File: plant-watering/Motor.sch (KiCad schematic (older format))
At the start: 3 parts, among them J5 Screw_Terminal_01x02, J6 Screw_Terminal_01x02, J7 Screw_Terminal_01x02

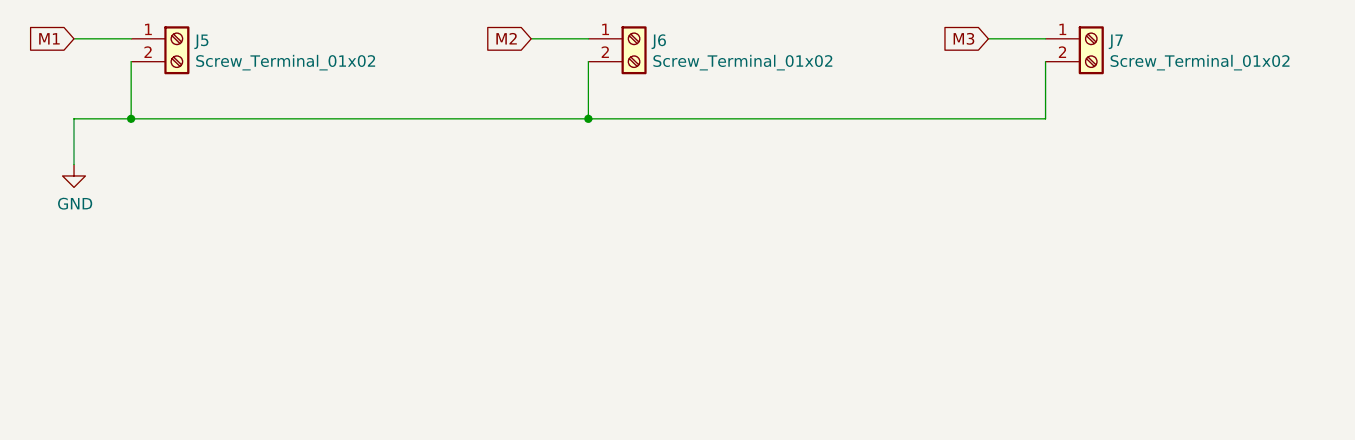
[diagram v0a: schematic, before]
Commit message: edited schematic & started pcb design
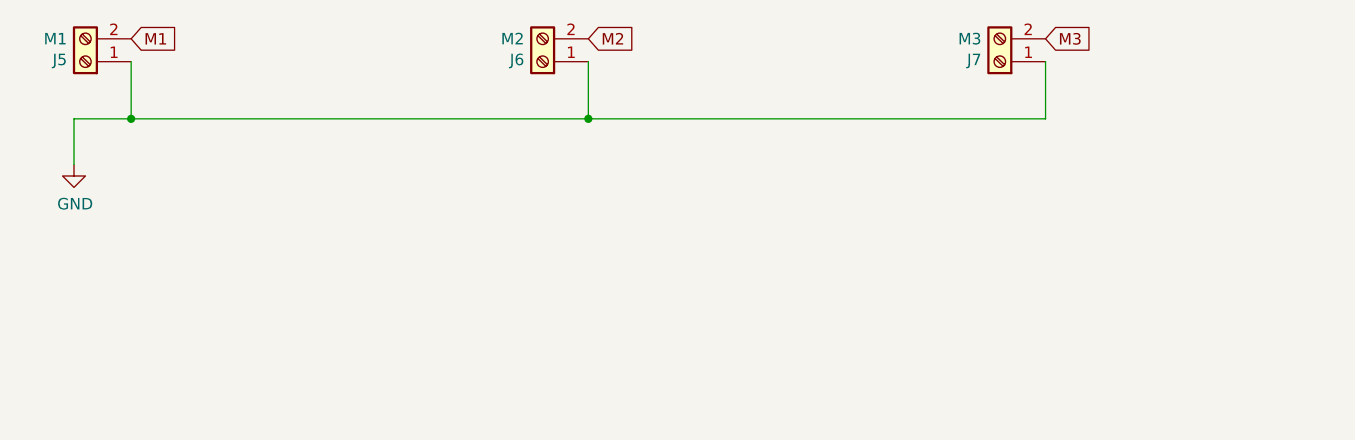
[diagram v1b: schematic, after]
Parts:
- J5: value Screw_Terminal_01x02 -> M1
- J6: value Screw_Terminal_01x02 -> M2
- J7: value Screw_Terminal_01x02 -> M3
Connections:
- net GND: now also J5.1 (Pin_1), J6.1 (Pin_1), J7.1 (Pin_1); no longer J5.2 (Pin_2), J6.2 (Pin_2), J7.2 (Pin_2)
- net M1: now also J5.2 (Pin_2); no longer J5.1 (Pin_1)
- net M2: now also J6.2 (Pin_2); no longer J6.1 (Pin_1)
- net M3: now also J7.2 (Pin_2); no longer J7.1 (Pin_1)
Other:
- moved on the sheet: J5, J6, J7
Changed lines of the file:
@@
 L Connector:Screw_Terminal_01x02 J5
 U 1 1 600B60F0
-P 4700 2900
-F 0 "J5" H 4780 2892 50  0000 L CNN
-F 1 "Screw_Terminal_01x02" H 4780 2801 50  0000 L CNN
-F 2 "Terminal_Blocks:TerminalBlock_bornier-2_P5.08mm" H 4700 2900 50  0001 C CNN
-F 3 "~" H 4700 2900 50  0001 C CNN
-	1    4700 2900
-	1    0    0    -1
+P 4300 3000
+F 0 "J5" H 4380 2992 50  0000 L CNN
+F 1 "M1" H 4380 2901 50  0000 L CNN
+F 2 "Terminal_Blocks:TerminalBlock_bornier-2_P5.08mm" H 4300 3000 50  0001 C CNN
+F 3 "~" H 4300 3000 50  0001 C CNN
+	1    4300 3000
+	-1   0    0    1
 $EndComp
 $Comp
 L Connector:Screw_Terminal_01x02 J6
 U 1 1 600B6A4A
-P 6700 2900
-F 0 "J6" H 6780 2892 50  0000 L CNN
-F 1 "Screw_Terminal_01x02" H 6780 2801 50  0000 L CNN
-F 2 "Terminal_Blocks:TerminalBlock_bornier-2_P5.08mm" H 6700 2900 50  0001 C CNN
-F 3 "~" H 6700 2900 50  0001 C CNN
-	1    6700 2900
-	1    0    0    -1
+P 6300 3000
+F 0 "J6" H 6380 2992 50  0000 L CNN
+F 1 "M2" H 6380 2901 50  0000 L CNN
+F 2 "Terminal_Blocks:TerminalBlock_bornier-2_P5.08mm" H 6300 3000 50  0001 C CNN
+F 3 "~" H 6300 3000 50  0001 C CNN
+	1    6300 3000
+	-1   0    0    1
 $EndComp
 $Comp
 L Connector:Screw_Terminal_01x02 J7
 U 1 1 600B7436
-P 8700 2900
-F 0 "J7" H 8780 2892 50  0000 L CNN
-F 1 "Screw_Terminal_01x02" H 8780 2801 50  0000 L CNN
-F 2 "Terminal_Blocks:TerminalBlock_bornier-2_P5.08mm" H 8700 2900 50  0001 C CNN
-F 3 "~" H 8700 2900 50  0001 C CNN
-	1    8700 2900
-	1    0    0    -1
+P 8300 3000
+F 0 "J7" H 8380 2992 50  0000 L CNN
+F 1 "M3" H 8380 2901 50  0000 L CNN
+F 2 "Terminal_Blocks:TerminalBlock_bornier-2_P5.08mm" H 8300 3000 50  0001 C CNN
+F 3 "~" H 8300 3000 50  0001 C CNN
+	1    8300 3000
+	-1   0    0    1
 $EndComp
 Wire Wire Line
@@
 	1    0    0    -1
 $EndComp
-Text GLabel 4250 2900 0    50   Input ~ 0
+Text GLabel 4500 2900 2    50   Input ~ 0
 M1
-Text GLabel 6250 2900 0    50   Input ~ 0
+Text GLabel 6500 2900 2    50   Input ~ 0
 M2
-Text GLabel 8250 2900 0    50   Input ~ 0
+Text GLabel 8500 2900 2    50   Input ~ 0
 M3
-Wire Wire Line
-	8250 2900 8500 2900
-Wire Wire Line
-	6500 2900 6250 2900
-Wire Wire Line
-	4500 2900 4250 2900
 $EndSCHEMATC

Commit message: added several parts#
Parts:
- added J11: M1, Terminal_Blocks:TerminalBlock_bornier-2_P5.08mm, symbol Connector:Screw_Terminal_01x02
- added J12: M2, Terminal_Blocks:TerminalBlock_bornier-2_P5.08mm, symbol Connector:Screw_Terminal_01x02
- added J13: M3, Terminal_Blocks:TerminalBlock_bornier-2_P5.08mm, symbol Connector:Screw_Terminal_01x02
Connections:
- net GND: now also J11.1 (Pin_1), J12.1 (Pin_1), J13.1 (Pin_1)
- new net M4: J11.2 (Pin_2)
- new net M5: J12.2 (Pin_2)
- new net M6: J13.2 (Pin_2)
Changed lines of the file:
@@
 $Descr A4 11693 8268
 encoding utf-8
-Sheet 6 6
+Sheet 6 7
 Title ""
 Date ""
@@
 Text GLabel 8500 2900 2    50   Input ~ 0
 M3
+$Comp
+L Connector:Screw_Terminal_01x02 J11
+U 1 1 60129D25
+P 4300 3900
+F 0 "J11" H 4380 3892 50  0000 L CNN
+F 1 "M1" H 4380 3801 50  0000 L CNN
+F 2 "Terminal_Blocks:TerminalBlock_bornier-2_P5.08mm" H 4300 3900 50  0001 C CNN
+F 3 "~" H 4300 3900 50  0001 C CNN
+	1    4300 3900
+	-1   0    0    1
+$EndComp
+$Comp
+L Connector:Screw_Terminal_01x02 J12
+U 1 1 60129D2B
+P 6300 3900
+F 0 "J12" H 6380 3892 50  0000 L CNN
+F 1 "M2" H 6380 3801 50  0000 L CNN
+F 2 "Terminal_Blocks:TerminalBlock_bornier-2_P5.08mm" H 6300 3900 50  0001 C CNN
+F 3 "~" H 6300 3900 50  0001 C CNN
+	1    6300 3900
+	-1   0    0    1
+$EndComp
+$Comp
+L Connector:Screw_Terminal_01x02 J13
+U 1 1 60129D31
+P 8300 3900
+F 0 "J13" H 8380 3892 50  0000 L CNN
+F 1 "M3" H 8380 3801 50  0000 L CNN
+F 2 "Terminal_Blocks:TerminalBlock_bornier-2_P5.08mm" H 8300 3900 50  0001 C CNN
+F 3 "~" H 8300 3900 50  0001 C CNN
+	1    8300 3900
+	-1   0    0    1
+$EndComp
+Wire Wire Line
+	8500 3900 8500 4150
+Wire Wire Line
+	8500 4150 6500 4150
+Wire Wire Line
+	4500 3900 4500 4150
+Connection ~ 4500 4150
+Wire Wire Line
+	4500 4150 4250 4150
+Wire Wire Line
+	6500 3900 6500 4150
+Connection ~ 6500 4150
+Wire Wire Line
+	6500 4150 4500 4150
+Wire Wire Line
+	4250 4150 4250 4350
+$Comp
+L power:GND #PWR0112
+U 1 1 60129D40
+P 4250 4350
+F 0 "#PWR0112" H 4250 4100 50  0001 C CNN
+F 1 "GND" H 4255 4177 50  0000 C CNN
+F 2 "" H 4250 4350 50  0001 C CNN
+F 3 "" H 4250 4350 50  0001 C CNN
+	1    4250 4350
+	1    0    0    -1
+$EndComp
+Text GLabel 4500 3800 2    50   Input ~ 0
+M4
+Text GLabel 6500 3800 2    50   Input ~ 0
+M5
+Text GLabel 8500 3800 2    50   Input ~ 0
+M6
 $EndSCHEMATC

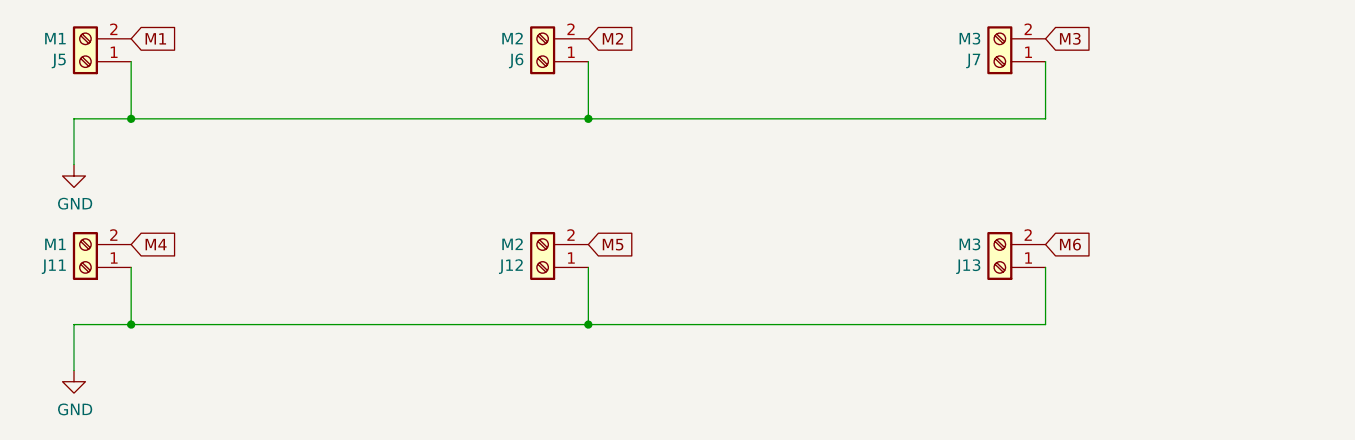
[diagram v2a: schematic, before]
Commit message: changed pcb parts
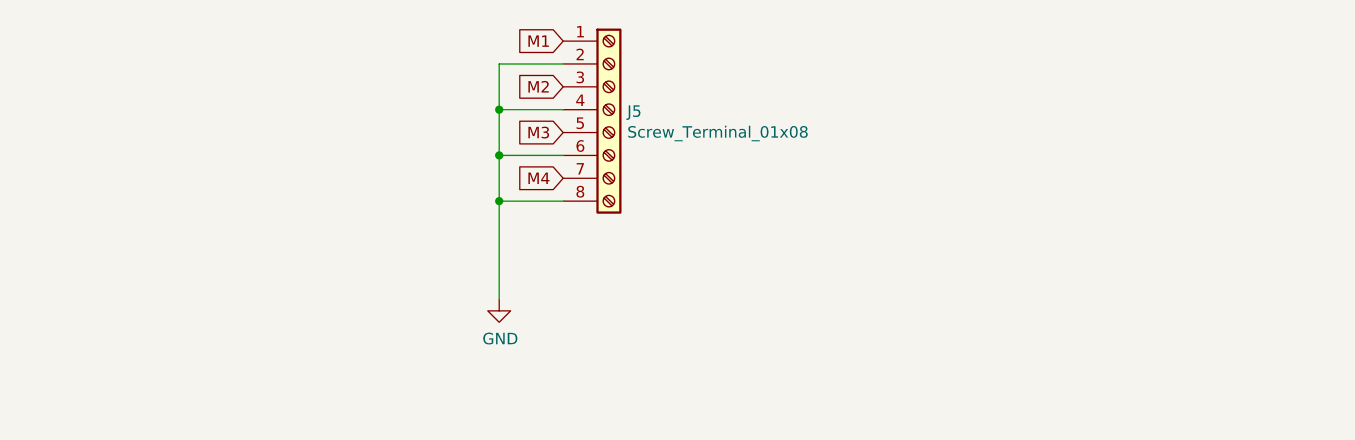
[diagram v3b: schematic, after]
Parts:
- removed J11, J5: M1, Terminal_Blocks:TerminalBlock_bornier-2_P5.08mm, symbol Connector:Screw_Terminal_01x02
- removed J12, J6: M2, Terminal_Blocks:TerminalBlock_bornier-2_P5.08mm, symbol Connector:Screw_Terminal_01x02
- removed J13, J7: M3, Terminal_Blocks:TerminalBlock_bornier-2_P5.08mm, symbol Connector:Screw_Terminal_01x02
- added J5: Screw_Terminal_01x08, TerminalBlock:ScrewTerminal_1x8_P5.00, symbol Connector:Screw_Terminal_01x08
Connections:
- net GND: now also J5.2 (Pin_2), J5.4 (Pin_4), J5.6 (Pin_6), J5.8 (Pin_8)
- net M1: now also J5.1 (Pin_1)
- net M2: now also J5.3 (Pin_3)
- net M3: now also J5.5 (Pin_5)
- net M4: now also J5.7 (Pin_7)
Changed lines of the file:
@@
 Comment4 ""
 $EndDescr
-$Comp
-L Connector:Screw_Terminal_01x02 J5
-U 1 1 600B60F0
-P 4300 3000
-F 0 "J5" H 4380 2992 50  0000 L CNN
-F 1 "M1" H 4380 2901 50  0000 L CNN
-F 2 "Terminal_Blocks:TerminalBlock_bornier-2_P5.08mm" H 4300 3000 50  0001 C CNN
-F 3 "~" H 4300 3000 50  0001 C CNN
-	1    4300 3000
-	-1   0    0    1
-$EndComp
-$Comp
-L Connector:Screw_Terminal_01x02 J6
-U 1 1 600B6A4A
-P 6300 3000
-F 0 "J6" H 6380 2992 50  0000 L CNN
-F 1 "M2" H 6380 2901 50  0000 L CNN
-F 2 "Terminal_Blocks:TerminalBlock_bornier-2_P5.08mm" H 6300 3000 50  0001 C CNN
-F 3 "~" H 6300 3000 50  0001 C CNN
-	1    6300 3000
-	-1   0    0    1
-$EndComp
-$Comp
-L Connector:Screw_Terminal_01x02 J7
-U 1 1 600B7436
-P 8300 3000
-F 0 "J7" H 8380 2992 50  0000 L CNN
-F 1 "M3" H 8380 2901 50  0000 L CNN
-F 2 "Terminal_Blocks:TerminalBlock_bornier-2_P5.08mm" H 8300 3000 50  0001 C CNN
-F 3 "~" H 8300 3000 50  0001 C CNN
-	1    8300 3000
-	-1   0    0    1
-$EndComp
-Wire Wire Line
-	8500 3000 8500 3250
-Wire Wire Line
-	8500 3250 6500 3250
-Wire Wire Line
-	4500 3000 4500 3250
-Connection ~ 4500 3250
-Wire Wire Line
-	4500 3250 4250 3250
-Wire Wire Line
-	6500 3000 6500 3250
-Connection ~ 6500 3250
-Wire Wire Line
-	6500 3250 4500 3250
-Wire Wire Line
-	4250 3250 4250 3450
-$Comp
-L power:GND #PWR0107
-U 1 1 600B8A6F
-P 4250 3450
-F 0 "#PWR0107" H 4250 3200 50  0001 C CNN
-F 1 "GND" H 4255 3277 50  0000 C CNN
-F 2 "" H 4250 3450 50  0001 C CNN
-F 3 "" H 4250 3450 50  0001 C CNN
-	1    4250 3450
-	1    0    0    -1
-$EndComp
-Text GLabel 4500 2900 2    50   Input ~ 0
+Text GLabel 6390 2910 0    50   Input ~ 0
 M1
-Text GLabel 6500 2900 2    50   Input ~ 0
+Text GLabel 6390 3110 0    50   Input ~ 0
 M2
-Text GLabel 8500 2900 2    50   Input ~ 0
+Text GLabel 6390 3310 0    50   Input ~ 0
 M3
-$Comp
-L Connector:Screw_Terminal_01x02 J11
-U 1 1 60129D25
-P 4300 3900
-F 0 "J11" H 4380 3892 50  0000 L CNN
-F 1 "M1" H 4380 3801 50  0000 L CNN
-F 2 "Terminal_Blocks:TerminalBlock_bornier-2_P5.08mm" H 4300 3900 50  0001 C CNN
-F 3 "~" H 4300 3900 50  0001 C CNN
-	1    4300 3900
-	-1   0    0    1
-$EndComp
-$Comp
-L Connector:Screw_Terminal_01x02 J12
-U 1 1 60129D2B
-P 6300 3900
-F 0 "J12" H 6380 3892 50  0000 L CNN
-F 1 "M2" H 6380 3801 50  0000 L CNN
-F 2 "Terminal_Blocks:TerminalBlock_bornier-2_P5.08mm" H 6300 3900 50  0001 C CNN
-F 3 "~" H 6300 3900 50  0001 C CNN
-	1    6300 3900
-	-1   0    0    1
-$EndComp
-$Comp
-L Connector:Screw_Terminal_01x02 J13
-U 1 1 60129D31
-P 8300 3900
-F 0 "J13" H 8380 3892 50  0000 L CNN
-F 1 "M3" H 8380 3801 50  0000 L CNN
-F 2 "Terminal_Blocks:TerminalBlock_bornier-2_P5.08mm" H 8300 3900 50  0001 C CNN
-F 3 "~" H 8300 3900 50  0001 C CNN
-	1    8300 3900
-	-1   0    0    1
-$EndComp
-Wire Wire Line
-	8500 3900 8500 4150
-Wire Wire Line
-	8500 4150 6500 4150
-Wire Wire Line
-	4500 3900 4500 4150
-Connection ~ 4500 4150
-Wire Wire Line
-	4500 4150 4250 4150
-Wire Wire Line
-	6500 3900 6500 4150
-Connection ~ 6500 4150
-Wire Wire Line
-	6500 4150 4500 4150
-Wire Wire Line
-	4250 4150 4250 4350
 $Comp
 L power:GND #PWR0112
 U 1 1 60129D40
-P 4250 4350
-F 0 "#PWR0112" H 4250 4100 50  0001 C CNN
-F 1 "GND" H 4255 4177 50  0000 C CNN
-F 2 "" H 4250 4350 50  0001 C CNN
-F 3 "" H 4250 4350 50  0001 C CNN
-	1    4250 4350
+P 6110 4040
+F 0 "#PWR0112" H 6110 3790 50  0001 C CNN
+F 1 "GND" H 6115 3867 50  0000 C CNN
+F 2 "" H 6110 4040 50  0001 C CNN
+F 3 "" H 6110 4040 50  0001 C CNN
+	1    6110 4040
 	1    0    0    -1
 $EndComp
-Text GLabel 4500 3800 2    50   Input ~ 0
+Text GLabel 6390 3510 0    50   Input ~ 0
 M4
-Text GLabel 6500 3800 2    50   Input ~ 0
-M5
-Text GLabel 8500 3800 2    50   Input ~ 0
-M6
+$Comp
+L Connector:Screw_Terminal_01x08 J5
+U 1 1 600EF051
+P 6590 3210
+F 0 "J5" H 6670 3202 50  0000 L CNN
+F 1 "Screw_Terminal_01x08" H 6670 3111 50  0000 L CNN
+F 2 "TerminalBlock:ScrewTerminal_1x8_P5.00" H 6590 3210 50  0001 C CNN
+F 3 "~" H 6590 3210 50  0001 C CNN
+	1    6590 3210
+	1    0    0    -1
+$EndComp
+Wire Wire Line
+	6390 3010 6110 3010
+Wire Wire Line
+	6110 3010 6110 3210
+Wire Wire Line
+	6390 3210 6110 3210
+Connection ~ 6110 3210
+Wire Wire Line
+	6110 3210 6110 3410
+Wire Wire Line
+	6390 3410 6110 3410
+Connection ~ 6110 3410
+Wire Wire Line
+	6110 3410 6110 3610
+Wire Wire Line
+	6390 3610 6110 3610
+Connection ~ 6110 3610
+Wire Wire Line
+	6110 3610 6110 4040
 $EndSCHEMATC
